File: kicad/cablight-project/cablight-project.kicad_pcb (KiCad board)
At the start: 4 copper layers, 71.4 x 40 mm, 62 parts, among them J3 Screw_Term_1x4_5mm, M2.5 MountingHole_2.7mm_M2.5_ISO73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, Q1 IRLB8721PBF, SW3 switch_SPDT_SLW_121586, T1 ISL85410, U1 TPD2EUSB30, U3 ESP32-S3-WROOM-1U

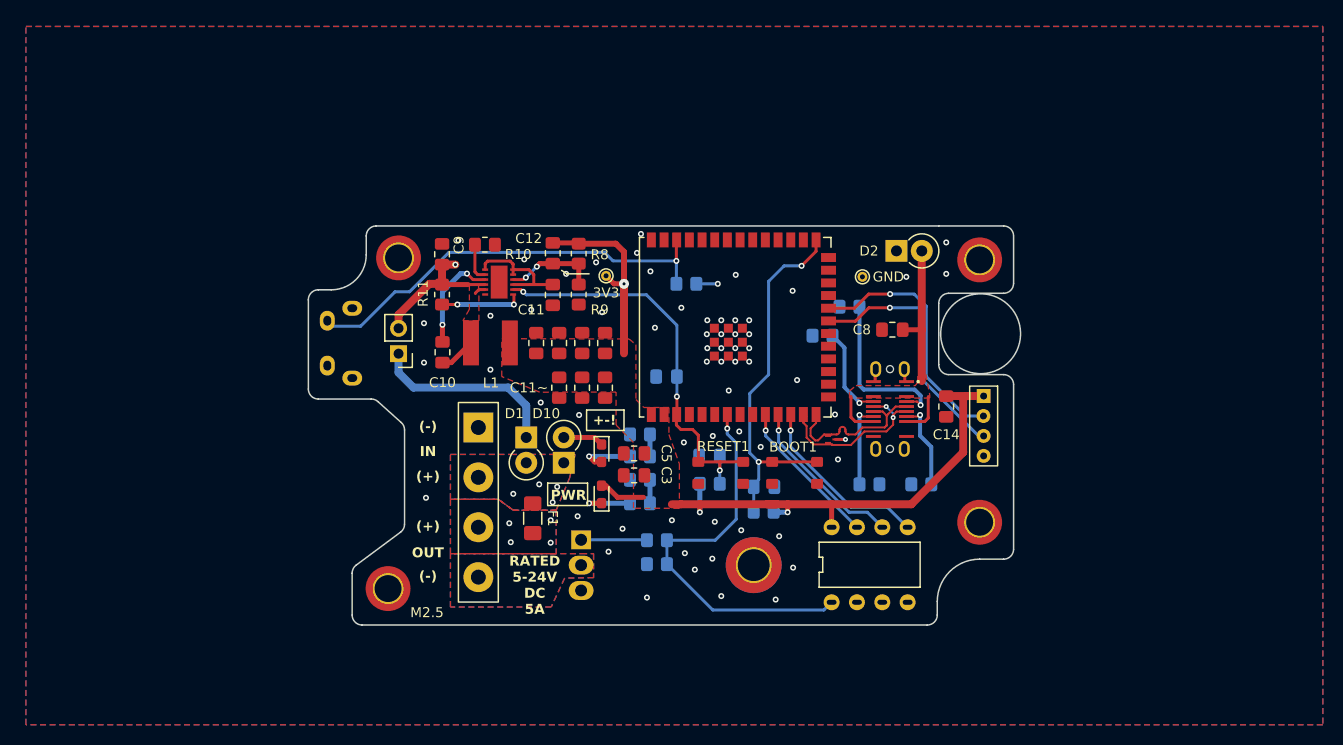
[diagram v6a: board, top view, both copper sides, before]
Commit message: create more space for usb esd
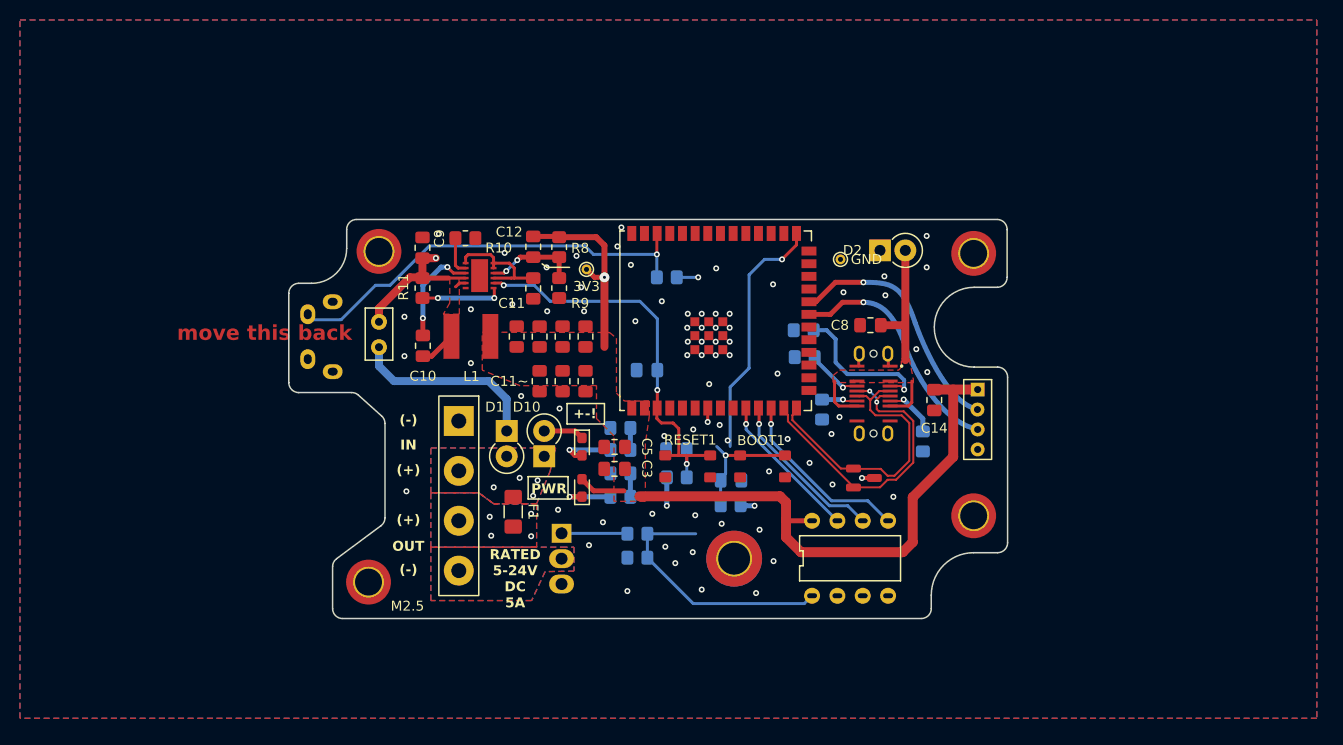
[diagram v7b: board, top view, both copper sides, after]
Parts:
- SW1: renamed from SW3; footprint Connector_PinHeader_2.54mm:PinHeader_1x02_P2.54mm_Vertical -> GRK_Lib:1x02_P2.54mm_Vertical_Shunt
- moved R6 8.88 mm to (107.5, 62.0), turned to -90 degrees
- moved U1 5.77 mm to (112.7, 68.9)
- moved R7 5.15 mm to (105.6, 54.1)
- moved R13 4.30 mm to (117.6, 65.2), turned to -90 degrees
- moved R3 3.37 mm to (92.9, 68.8)
- moved RESET1 3.37 mm to (96.2, 68.8)
- moved C7 3.37 mm to (98.3, 69.2)
- moved C6 3.37 mm to (92.9, 66.0)
- moved R2 3.37 mm to (98.3, 71.7)
- moved BOOT1 3.28 mm to (103.7, 68.8)
- moved TP2 2.81 mm to (109.3, 47.0)
- moved R12 2.80 mm to (105.7, 56.8)
- moved USBC-V1 2.26 mm to (112.6, 60.5)
- moved C8 2.25 mm to (112.3, 53.6)
- moved CP3 2.06 mm to (81.4, 54.7)
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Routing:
- net ECHO: track 25.6 -> 6.08 mm
- net TRIG: track 25.4 -> 6.31 mm
- net D-: track 17.6 -> 31.9 mm
- net LEDSIG: track 39.9 -> 27.5 mm
- net D+: track 16.4 -> 28.9 mm
- net 3.3V: track 86.9 -> 97.7 mm
- net Net-(USBC-V1-CC2): track 8.62 -> 3.77 mm
- net Net-(USBC-V1-SBU1): track 9.36 -> 5.59 mm
- net Net-(USBC-V1-SBU2): track 9.51 -> 5.87 mm
- net Net-(USBC-V1-CC1): track 17.1 -> 15.2 mm
- net /VBUS: track 24.3 -> 22.6 mm
- net 5V: track 60.1 -> 60.7 mm
- net GND: track 3.71 -> 3.95 mm, vias 62 -> 72
- net Net-(U3-GPIO0/BOOT): vias 2 -> 3
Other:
- board size 71.4 x 40 mm -> 72 x 40 mm
- board text added: "move this back"
- board text added: "need to make these holes line up with 0.1mm"

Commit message: schematic cleanup
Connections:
- DIP1 pad 1: LEDSIG -> GND
- DIP1 pad 8: 3.3V -> DIP0
- U3 pad 9: unconnected-(U3-GPIO16/U0CTS/ADC2_CH5/XTAL_32K_N-Pad9) -> DIP0
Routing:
- net DIP0: track 0.00 -> 14.6 mm, vias 0 -> 1
- net LEDSIG: track 27.5 -> 20.1 mm
- net Net-(U3-GPIO0/BOOT): track 37.6 -> 37.8 mm, vias 3 -> 2
- net GND: vias 72 -> 67
- net ECHO: vias 1 -> 3
